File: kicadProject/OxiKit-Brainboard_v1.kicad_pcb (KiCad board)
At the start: 2 copper layers, 100 x 100 mm, 60 parts, among them J1 OXY-Sensor, J10 Valve3, J11 Air Compresssor, J2 Jack-DC, J3 UART, J4 Fan1, J5 Fan2, J6 I2C, J7 Valve1, J8 Valve2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

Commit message: #1 ULN2003 and Relay connection Fixed, Indication LED of Relay also updated
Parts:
- turned D10 to 180 degrees
- turned D3 to 180 degrees
- turned D6 to 180 degrees
- turned D9 to 180 degrees
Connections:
- D10 pad 1: Net-(D10-Pad1) -> O3
- D10 pad 2: O3 -> Net-(R8-Pad1)
- D3 pad 1: Net-(D3-Pad1) -> O1
- D3 pad 2: O1 -> Net-(R5-Pad1)
- D6 pad 1: Net-(D6-Pad1) -> O2
- D6 pad 2: O2 -> Net-(D6-Pad2)
- D9 pad 1: Net-(D9-Pad1) -> O4
- D9 pad 2: O4 -> Net-(R7-Pad1)
- K1 pad A1: GND -> +5V
- K2 pad A1: GND -> +5V
- K3 pad A1: GND -> +5V
- K4 pad A1: GND -> +5V
- R5 pad 1: Net-(D3-Pad1) -> Net-(R5-Pad1)
- R5 pad 2: GND -> +5V
- R6 pad 1: Net-(D6-Pad1) -> Net-(D6-Pad2)
- R6 pad 2: GND -> +5V
- R7 pad 1: Net-(D9-Pad1) -> Net-(R7-Pad1)
- R7 pad 2: GND -> +5V
- R8 pad 1: Net-(D10-Pad1) -> Net-(R8-Pad1)
- R8 pad 2: GND -> +5V
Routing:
- net +5V: track 307.0 -> 438.9 mm
- net Net-(R8-Pad1): track 0.00 -> 3.26 mm
- net Net-(R7-Pad1): track 0.00 -> 3.26 mm
- net Net-(R5-Pad1): track 0.00 -> 3.26 mm
- net Net-(D9-Pad1): track 3.26 -> 0.00 mm
- net Net-(D6-Pad2): track 0.00 -> 3.26 mm
- net Net-(D6-Pad1): track 3.26 -> 0.00 mm
- net Net-(D3-Pad1): track 3.26 -> 0.00 mm
- net Net-(D10-Pad1): track 3.26 -> 0.00 mm
- net O2: track 16.2 -> 15.3 mm
- net GND: vias 124 -> 105

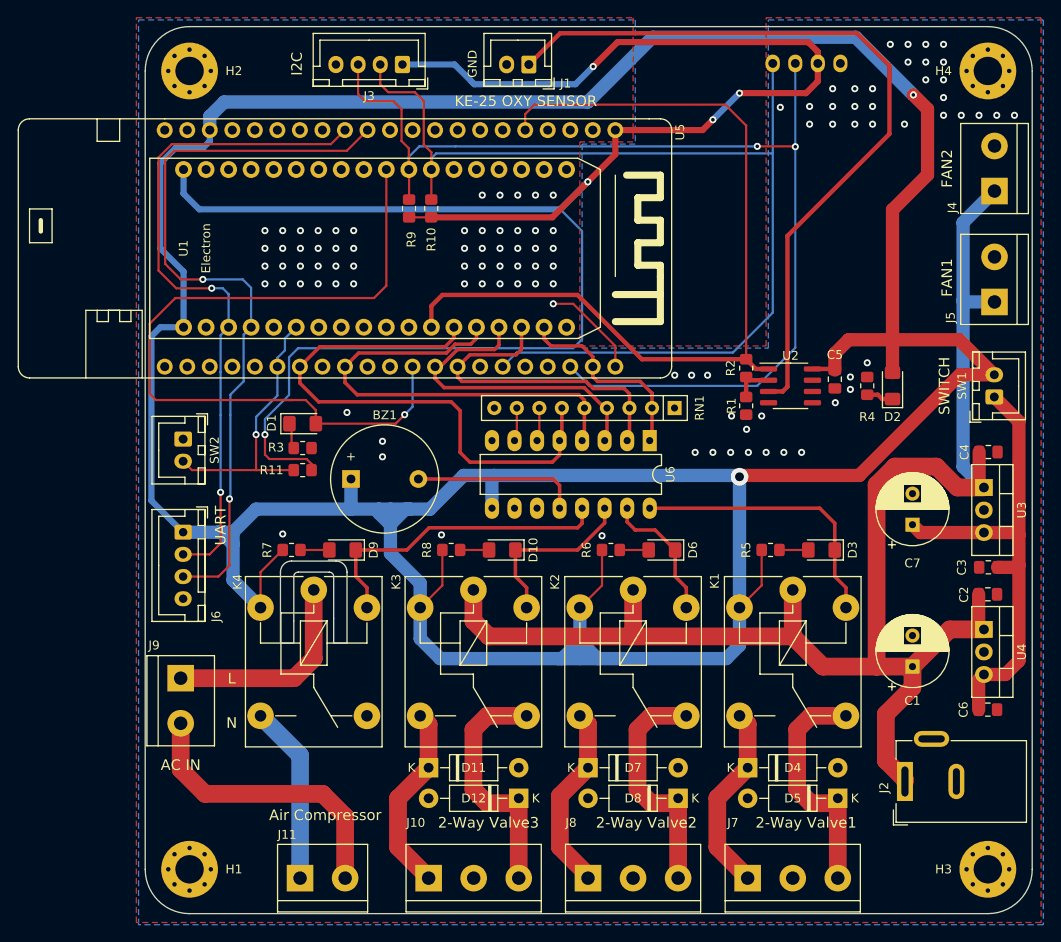
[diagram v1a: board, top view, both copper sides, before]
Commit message: OSHW Logo Added
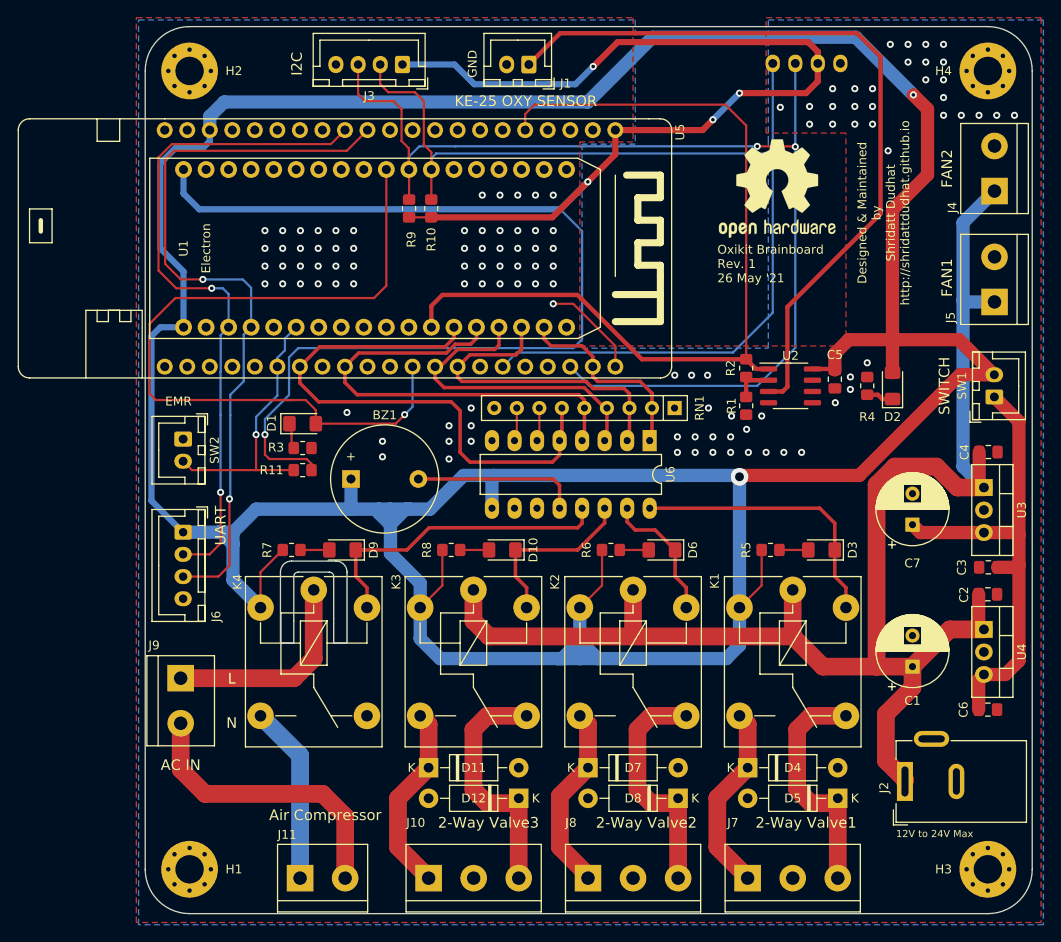
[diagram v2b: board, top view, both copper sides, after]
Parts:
- added REF**: OSHW-Logo2_14.6x12mm_SilkScreen, Symbol:OSHW-Logo2_14.6x12mm_SilkScreen, F.Cu at (121.2, 58.2)
- added REF**: OSHW-Logo2_14.6x12mm_SilkScreen, Symbol:OSHW-Logo2_14.6x12mm_SilkScreen, B.Cu at (124.5, 78.0)
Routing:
- net Net-(J1-Pad1): track 86.9 -> 86.1 mm
- net GND: vias 105 -> 114
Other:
- board text added: "12V to 24V Max"
- board text added: "Designed & Maintained by Shridatt Dudhat http://shridattdudhat.github.io"
- board text added: "EMR"
- board text added: "Oxikit Brainboard Rev. 1 26 May '21"

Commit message: ABP Honeywell Pressure Sensor added
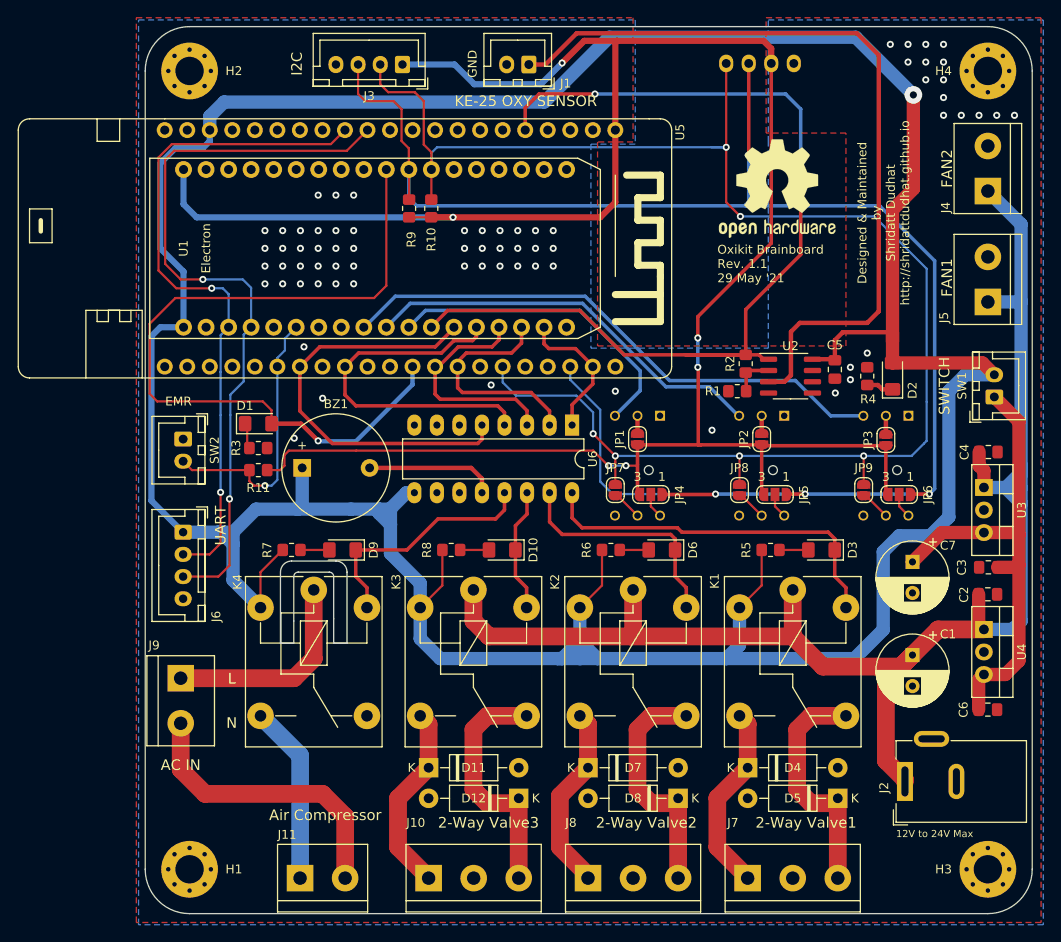
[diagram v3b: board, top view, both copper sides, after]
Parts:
- removed RN1: R_Network08, Resistor_THT:R_Array_SIP9
- added JP1: SolderJumper_2_Open, Jumper:SolderJumper-2_P1.3mm_Open_RoundedPad1.0x1.5mm, F.Cu at (105.5, 86.5)
- added JP2: SolderJumper_2_Open, Jumper:SolderJumper-2_P1.3mm_Open_RoundedPad1.0x1.5mm, F.Cu at (119.5, 86.5)
- added JP3: SolderJumper_2_Open, Jumper:SolderJumper-2_P1.3mm_Open_RoundedPad1.0x1.5mm, F.Cu at (133.5, 86.6)
- added JP4: SolderJumper_3_Open, Jumper:SolderJumper-3_P1.3mm_Open_RoundedPad1.0x1.5mm_NumberLabels, F.Cu at (107.0, 92.8)
- added JP5: SolderJumper_3_Open, Jumper:SolderJumper-3_P1.3mm_Open_RoundedPad1.0x1.5mm_NumberLabels, F.Cu at (121.0, 92.8)
- added JP6: SolderJumper_3_Open, Jumper:SolderJumper-3_P1.3mm_Open_RoundedPad1.0x1.5mm_NumberLabels, F.Cu at (135.0, 92.8)
- added JP7: SolderJumper_2_Open, Jumper:SolderJumper-2_P1.3mm_Open_RoundedPad1.0x1.5mm, F.Cu at (103.0, 92.2)
- added JP8: SolderJumper_2_Open, Jumper:SolderJumper-2_P1.3mm_Open_RoundedPad1.0x1.5mm, F.Cu at (117.0, 92.2)
- added JP9: SolderJumper_2_Open, Jumper:SolderJumper-2_P1.3mm_Open_RoundedPad1.0x1.5mm, F.Cu at (131.0, 92.2)
- added PS1: ABP-Honeywell, OxiKit-footprint-lib:ABP-Series-Pressure, B.Cu at (105.5, 89.5)
- added PS2: ABP-Honeywell, OxiKit-footprint-lib:ABP-Series-Pressure, B.Cu at (119.5, 89.5)
- added PS3: ABP-Honeywell, OxiKit-footprint-lib:ABP-Series-Pressure, B.Cu at (133.5, 89.5)
- moved REF** 40.1 mm to (86.6, 64.8), turned to 90 degrees
- moved U6 8.92 mm to (98.1, 84.9)
- moved BZ1 5.64 mm to (67.7, 89.8)
- moved Brd1 5.25 mm to (119.5, 54.8)
- moved D1 5.00 mm to (62.8, 84.8)
- moved R11 5.00 mm to (62.8, 90.0)
- moved R3 5.00 mm to (62.8, 87.5)
- moved C7 4.19 mm to (136.5, 100.3), turned to -90 degrees
- moved R1 1.93 mm to (116.8, 81.1), turned to 0 degrees
- moved C1 1.31 mm to (136.5, 110.8), turned to -90 degrees
- moved C5 1.09 mm to (127.8, 78.7)
- moved D2 1.09 mm to (134.2, 79.4)
- moved R4 1.09 mm to (131.4, 79.4)
- moved U2 1.09 mm to (122.8, 79.4)
- moved J4 0.75 mm to (145.0, 58.5)
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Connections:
- K4 pad 12: (no net) -> unconnected-(K4-Pad12)
- U1 pad 10: (no net) -> PS2
- U1 pad 11: (no net) -> PS1
- U1 pad 18: (no net) -> unconnected-(U1-Pad18)
- U1 pad 19: (no net) -> unconnected-(U1-Pad19)
- U1 pad 20: (no net) -> unconnected-(U1-Pad20)
- U1 pad 21: (no net) -> unconnected-(U1-Pad21)
- U1 pad 22: (no net) -> unconnected-(U1-Pad22)
- U1 pad 23: (no net) -> unconnected-(U1-Pad23)
- U1 pad 24: (no net) -> unconnected-(U1-Pad24)
- U1 pad 28: (no net) -> unconnected-(U1-Pad28)
- U1 pad 29: (no net) -> unconnected-(U1-Pad29)
- U1 pad 30: (no net) -> unconnected-(U1-Pad30)
- U1 pad 31: (no net) -> unconnected-(U1-Pad31)
- U1 pad 32: (no net) -> unconnected-(U1-Pad32)
- U1 pad 34: (no net) -> unconnected-(U1-Pad34)
- U1 pad 35: (no net) -> unconnected-(U1-Pad35)
- U1 pad 5: (no net) -> unconnected-(U1-Pad5)
- U1 pad 7: (no net) -> unconnected-(U1-Pad7)
- U1 pad 8: (no net) -> unconnected-(U1-Pad8)
- U1 pad 9: (no net) -> PS3
- U5 pad 10: (no net) -> unconnected-(U5-Pad10)
- U5 pad 11: (no net) -> unconnected-(U5-Pad11)
- U5 pad 15: (no net) -> unconnected-(U5-Pad15)
- U5 pad 16: (no net) -> unconnected-(U5-Pad16)
- U5 pad 17: (no net) -> unconnected-(U5-Pad17)
- U5 pad 18: (no net) -> unconnected-(U5-Pad18)
- U5 pad 2: (no net) -> unconnected-(U5-Pad2)
- U5 pad 20: (no net) -> unconnected-(U5-Pad20)
- U5 pad 21: (no net) -> unconnected-(U5-Pad21)
- U5 pad 25: (no net) -> unconnected-(U5-Pad25)
- U5 pad 26: (no net) -> unconnected-(U5-Pad26)
- U5 pad 3: (no net) -> unconnected-(U5-Pad3)
- U5 pad 32: (no net) -> unconnected-(U5-Pad32)
- U5 pad 33: (no net) -> unconnected-(U5-Pad33)
- U5 pad 35: (no net) -> unconnected-(U5-Pad35)
- U5 pad 38: (no net) -> unconnected-(U5-Pad38)
- U5 pad 39: (no net) -> unconnected-(U5-Pad39)
- U5 pad 4: (no net) -> unconnected-(U5-Pad4)
- U5 pad 40: (no net) -> unconnected-(U5-Pad40)
- U5 pad 41: (no net) -> unconnected-(U5-Pad41)
- U5 pad 42: (no net) -> unconnected-(U5-Pad42)
- U5 pad 6: (no net) -> unconnected-(U5-Pad6)
- U5 pad 7: (no net) -> unconnected-(U5-Pad7)
- U5 pad 8: (no net) -> unconnected-(U5-Pad8)
- U5 pad 9: (no net) -> unconnected-(U5-Pad9)
- U6 pad 10: (no net) -> O7
- U6 pad 11: (no net) -> O6
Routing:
- net SCL: track 125.1 -> 191.1 mm, vias 2 -> 4
- net PS3: track 0.00 -> 63.3 mm
- net SDA: track 120.4 -> 181.9 mm, vias 0 -> 6
- net PS2: track 0.00 -> 46.1 mm
- net +5V: track 438.9 -> 402.3 mm, vias 2 -> 1
- net PS1: track 0.00 -> 35.9 mm
- net +3.3V: track 225.9 -> 259.3 mm, vias 5 -> 6
- net I5: track 63.2 -> 48.1 mm
- net Oxy-out: track 98.9 -> 113.1 mm, vias 0 -> 2
- net I2: track 37.2 -> 25.8 mm
- net GND: track 11.3 -> 0.00 mm, vias 114 -> 70
- net O2: track 15.3 -> 26.5 mm
- net I4: track 51.7 -> 40.7 mm
- net I3: track 36.1 -> 25.7 mm
- net O1: track 31.6 -> 41.7 mm
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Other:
- board text added: "Oxikit Brainboard Rev. 1.1 29 May '21"
- board text added: "Oxygen Serge Tank"
- board text added: "Zeolite Bed A"
- board text added: "Zeolite Bed B"
- board text removed: "Oxikit Brainboard Rev. 1 26 May '21"

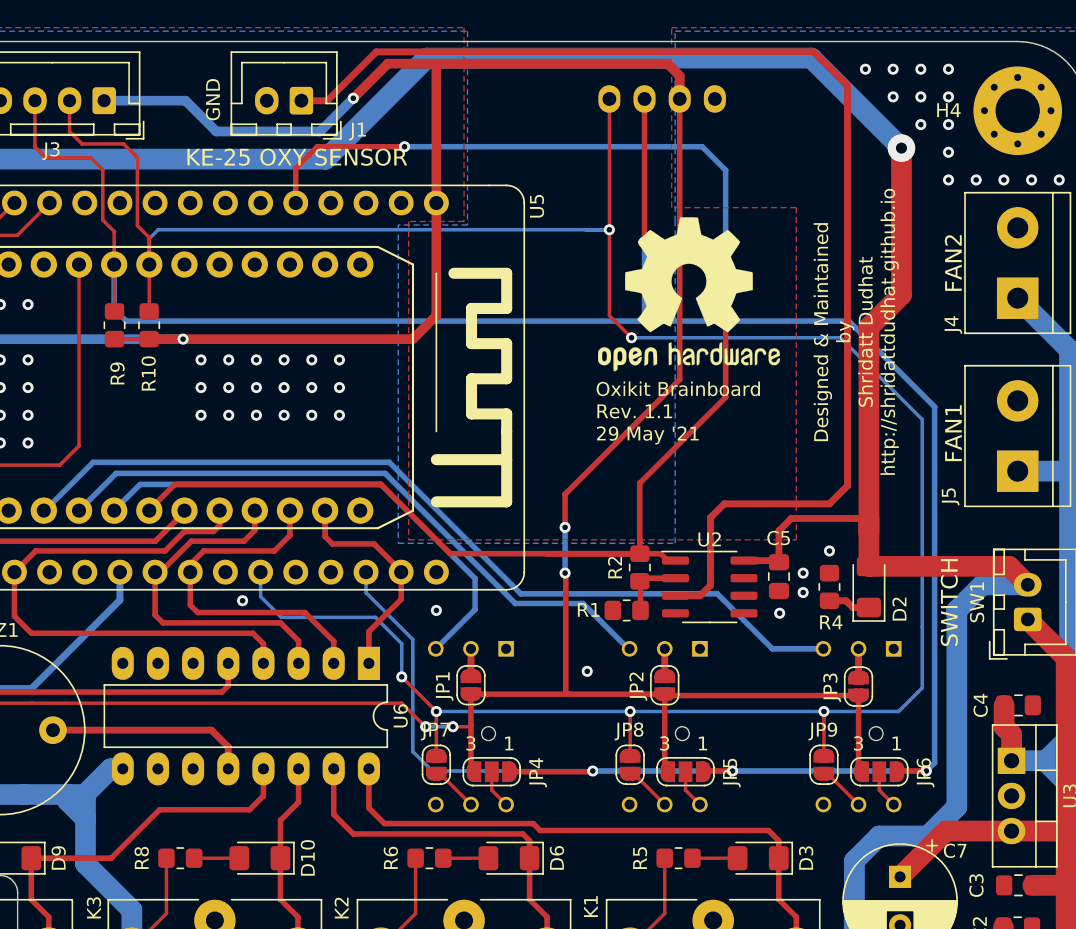
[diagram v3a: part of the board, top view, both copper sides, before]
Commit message: Pressure Sensor connection to ESP32 #2
PS1 >> IO25
PS2 >> IO26
PS3 >> IO27
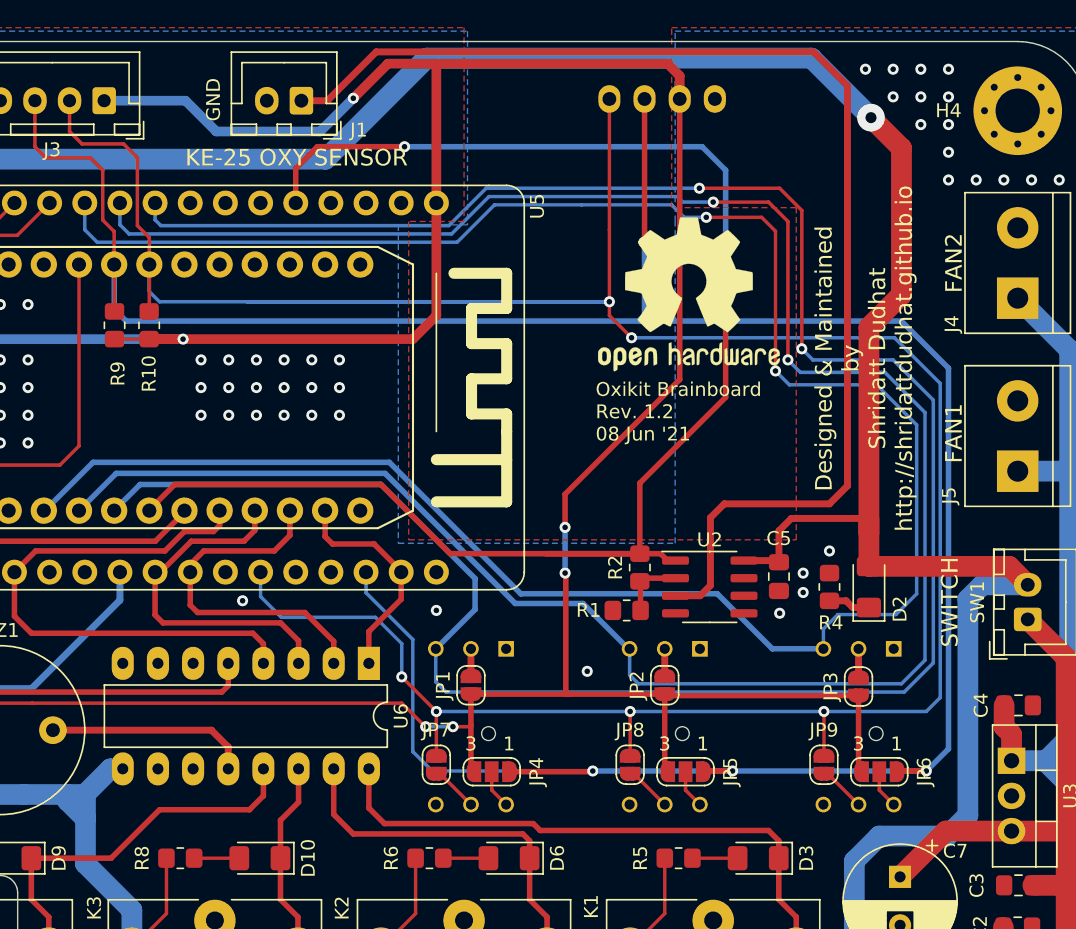
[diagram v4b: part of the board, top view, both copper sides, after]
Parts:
- removed the REF** at (86.6, 64.8)
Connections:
- U5 pad 10: unconnected-(U5-Pad10) -> PS2
- U5 pad 11: unconnected-(U5-Pad11) -> PS3
- U5 pad 9: unconnected-(U5-Pad9) -> PS1
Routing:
- net PS1: track 35.9 -> 165.4 mm, vias 0 -> 2
- net PS2: track 46.1 -> 161.7 mm, vias 0 -> 2
- net PS3: track 63.3 -> 160.8 mm, vias 0 -> 2
- net SDA: track 181.9 -> 211.1 mm
- net SCL: track 191.1 -> 194.1 mm
- net +5V: track 402.3 -> 403.1 mm
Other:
- board text added: "Oxikit Brainboard Rev. 1.2 08 Jun '21"
- board text removed: "Oxikit Brainboard Rev. 1.1 29 May '21"
